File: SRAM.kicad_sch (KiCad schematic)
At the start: 8 parts, among them U6 AS6C1616

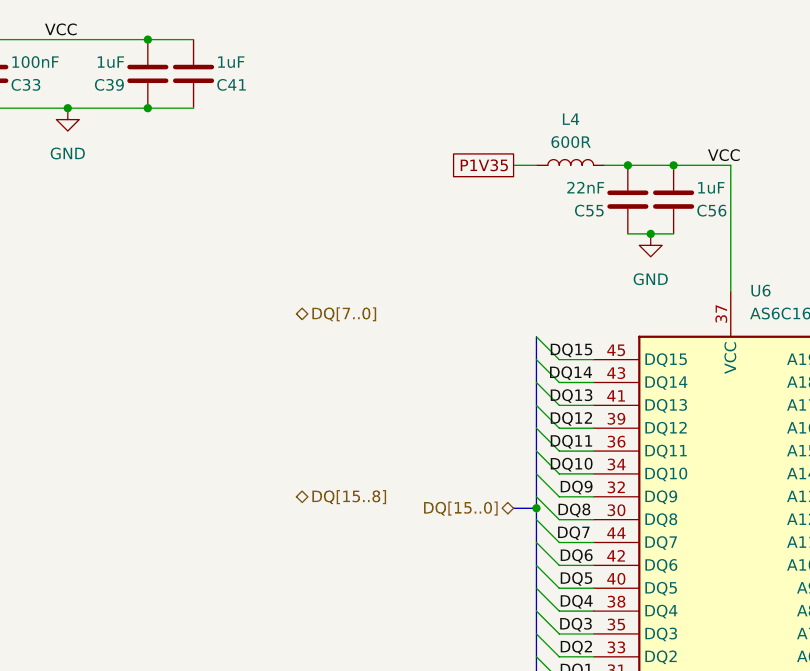
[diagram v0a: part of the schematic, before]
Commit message: Added more I/O. Changed power regulators
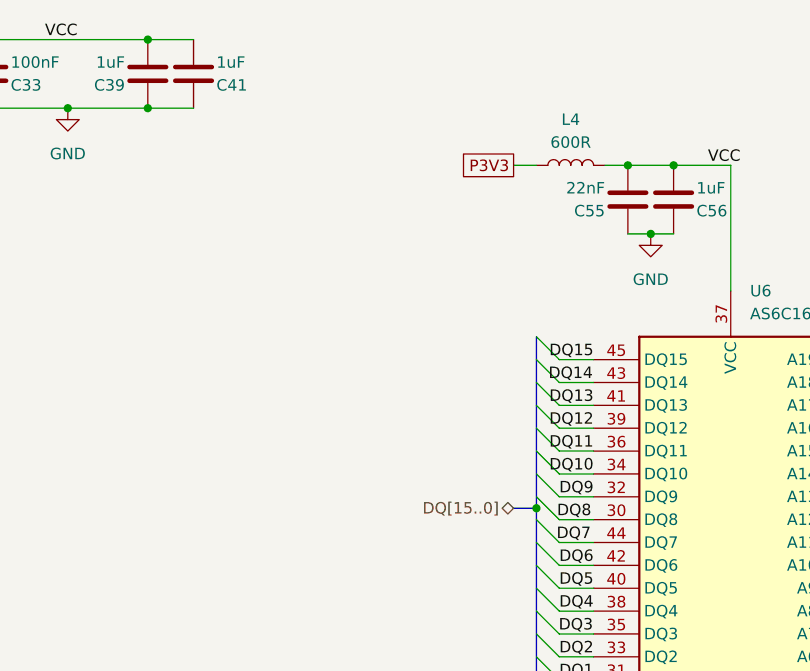
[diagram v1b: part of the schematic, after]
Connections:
- net P1V35 renamed P3V3
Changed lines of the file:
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@@
 		)
 	)
-	(global_label "P1V35"
+	(global_label "P3V3"
 		(shape passive)
 		(at 119.38 53.34 180)
@@
 		)
 		(property "Intersheetrefs" "${INTERSHEET_REFS}"
-			(at 111.519 53.34 0)
+			(at 112.7285 53.34 0)
 			(effects
 				(font
@@
 		)
 	)
-	(hierarchical_label "DQ[15..8]"
-		(shape bidirectional)
-		(at 95.25 90.17 0)
-		(effects
-			(font
-				(size 1.27 1.27)
-			)
-			(justify left)
-		)
-	)
 	(hierarchical_label "SRAM_CE2"
 		(shape input)
@@
 		)
 	)
-	(hierarchical_label "DQ[7..0]"
-		(shape bidirectional)
-		(at 95.25 69.85 0)
-		(effects
-			(font
-				(size 1.27 1.27)
-			)
-			(justify left)
-		)
-	)
 	(hierarchical_label "SRAM_WE_B"
 		(shape input)
@@
 		)
 		(instances
-			(project ""
+			(project "sbc"
 				(path "/9328a39f-e46f-4e23-a67b-f837d10a1254/ead0e1f6-3bed-4a4d-ba2e-bcbc99eccbe8/473a3989-8d64-4465-9744-9671bd8b9561"
 					(reference "U6")

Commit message: Power routed. Saving before reworking ICE40 pins to optimize layout
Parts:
- C15, C33, C39, C41, C55, C56: footprint (none) -> Capacitor_SMD:C_0603_1608Metric
- L4: footprint (none) -> Inductor_SMD:L_0603_1608Metric
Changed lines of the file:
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@@
 			)
 		)
-		(property "Footprint" ""
+		(property "Footprint" "Capacitor_SMD:C_0603_1608Metric"
 			(at 84.7852 46.99 0)
 			(effects
@@
 			)
 		)
-		(property "Footprint" ""
+		(property "Footprint" "Capacitor_SMD:C_0603_1608Metric"
 			(at 79.7052 46.99 0)
 			(effects
@@
 			)
 		)
-		(property "Footprint" ""
+		(property "Footprint" "Capacitor_SMD:C_0603_1608Metric"
 			(at 61.9252 46.99 0)
 			(effects
@@
 			)
 		)
-		(property "Footprint" ""
+		(property "Footprint" "Capacitor_SMD:C_0603_1608Metric"
 			(at 56.8452 46.99 0)
 			(effects
@@
 			)
 		)
-		(property "Footprint" ""
+		(property "Footprint" "Capacitor_SMD:C_0603_1608Metric"
 			(at 133.0452 60.96 0)
 			(effects
@@
 			)
 		)
-		(property "Footprint" ""
+		(property "Footprint" "Capacitor_SMD:C_0603_1608Metric"
 			(at 138.1252 60.96 0)
 			(effects
@@
 			)
 		)
-		(property "Footprint" ""
+		(property "Footprint" "Inductor_SMD:L_0603_1608Metric"
 			(at 125.73 53.34 0)
 			(effects
